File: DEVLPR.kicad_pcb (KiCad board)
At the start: 2 copper layers, 68.6 x 53.3 mm, 53 parts, among them CON1 SJ-3523-SMT-TR, J1 Conn_02x08_Row_Letter_Last, P1 Power, P2 Analog, P3 Digital, P4 Digital, P5 CONN_01X01, P6 CONN_01X01, P7 CONN_01X01, P8 CONN_01X01, U1 OPA140DGK, U2 INA333AIDGKR, U3 OPA376xxD, U4 TLV9002IPWR, U5 LM27761

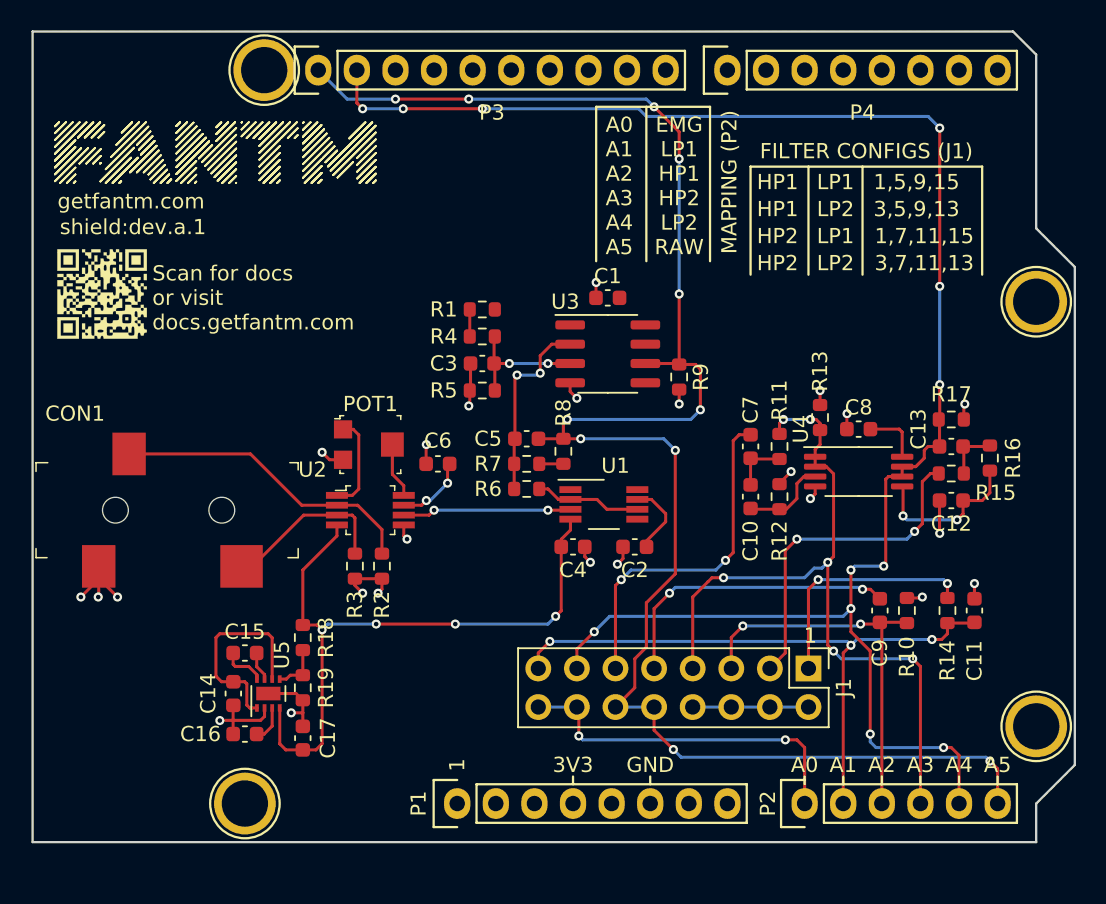
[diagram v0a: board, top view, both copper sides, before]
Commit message: Finalized rev dev.a.2 with improved filtering, power supply design, and silkscreen
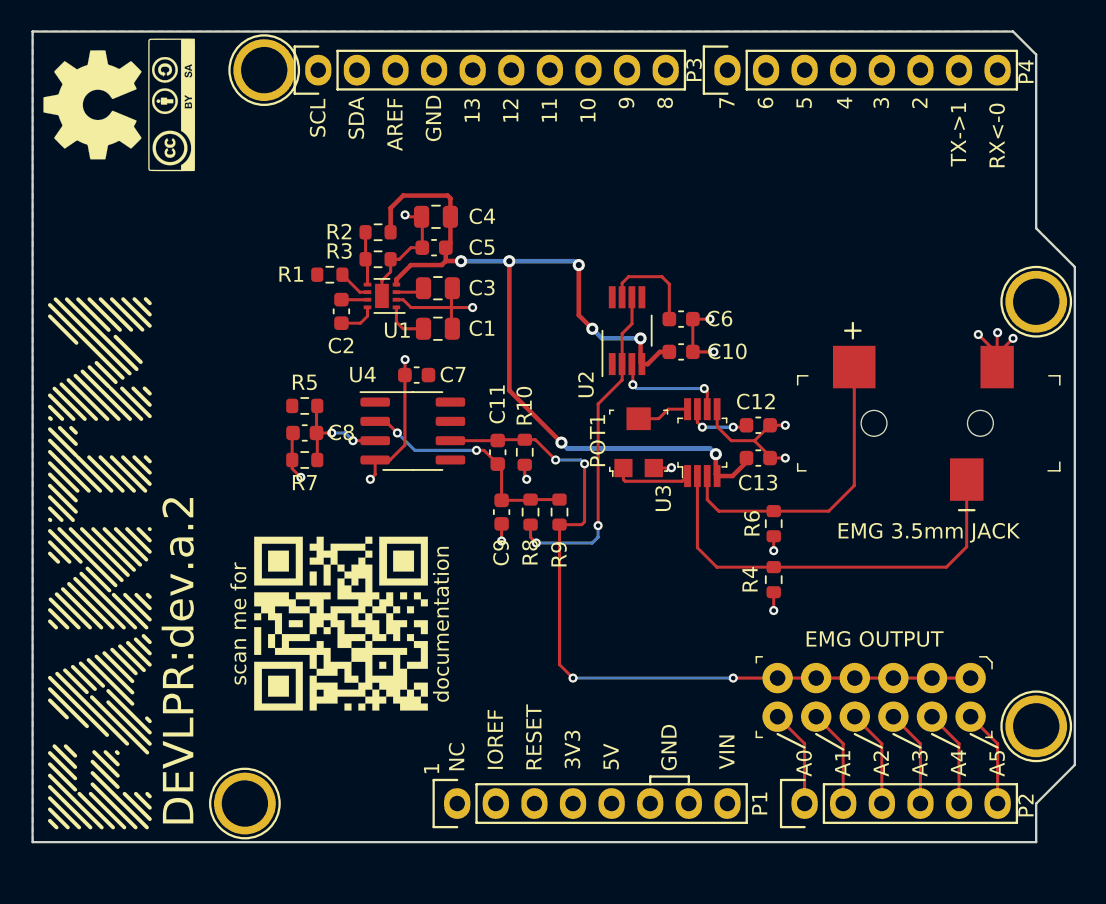
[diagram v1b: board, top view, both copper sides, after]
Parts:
- removed C14, C16: 4.7uF, Capacitor_SMD:C_0603_1608Metric
- removed C15: 1uF, Capacitor_SMD:C_0603_1608Metric
- removed C17: 2.2uF, Capacitor_SMD:C_0603_1608Metric
- removed the G*** at (115.6, 90.3)
- removed R11, R12, R19: 100k, Resistor_SMD:R_0603_1608Metric
- removed R13, R14, R15, R16, R17: 10k, Resistor_SMD:R_0603_1608Metric
- removed R18: 309k, Resistor_SMD:R_0603_1608Metric
- removed U5: LM27761, Package_SON:WSON-8-1EP_2x2mm_P0.5mm_EP0.9x1.6mm
- added G***: LOGO, kicad:qrcode_big, F.Cu at (131.3, 112.0)
- added G***: LOGO, kicad:cc_smlst, F.Cu at (120.1, 77.9)
- added G***: LOGO, kicad:oh_smlst, F.Cu at (114.9, 77.9)
- C1, C4: value 0.1uF -> 10uF; footprint Capacitor_SMD:C_0603_1608Metric -> Capacitor_SMD:C_0805_2012Metric
- C10, C7: value 0.15uF -> 0.1uF
- C11: value 0.033uF -> 4700pF
- C12, C13: value 0.033uF -> 0.1uF
- C2, C8: value 0.1uF -> 1uF
- C3: value 1uF -> 10uF; footprint Capacitor_SMD:C_0603_1608Metric -> Capacitor_SMD:C_0805_2012Metric
- C5: value 43pF -> 1uF
- C9: value 0.15uF -> 4700pF
- CON1: value SJ-3523-SMT-TR -> EMG 3.5mm JACK
- J1: value Conn_02x08_Row_Letter_Last -> EMG OUTPUT; footprint Connector_PinHeader_2.54mm:PinHeader_2x08_P2.54mm_Vertical -> digikey-footprints:PinHeader_6x2_P2.54mm_Horizontal
- POT1: value TC33X-2-103E -> GAIN
- R1: value 33k -> 100k
- R10: value 100k -> 10k
- R2: value 47k -> 182k
- R3: value 47k -> 100k
- R4: value 3.9k -> 47k
- R5: value 10k -> 36.5k
- R6: value 39k -> 47k
- R7: value 33k -> 10k
- R8: value 2.7k -> 39k
- R9: value 10k -> 35.7k
- U1: value OPA140DGK -> LM27761; footprint Package_SO:VSSOP-8_3.0x3.0mm_P0.65mm -> Package_SON:WSON-8-1EP_2x2mm_P0.5mm_EP0.9x1.6mm
- U2: value INA333AIDGKR -> OPA140DGK; footprint digikey-footprints:TSSOP-8_W3mm -> Package_SO:VSSOP-8_3.0x3.0mm_P0.65mm
- U3: value OPA376xxD -> INA333AIDGKR; footprint Package_SO:SOIC-8_3.9x4.9mm_P1.27mm -> digikey-footprints:TSSOP-8_W3mm
- U4: value TLV9002IPWR -> OPA376xxD; footprint Package_SO:TSSOP-8_4.4x3mm_P0.65mm -> Package_SO:SOIC-8_3.9x4.9mm_P1.27mm
- moved CON1 55.4 mm to (172.5, 98.8), turned to 180 degrees
- moved C8 36.4 mm to (128.9, 99.4)
- moved C11 33.1 mm to (141.6, 100.7)
- moved U4 29.5 mm to (136.0, 99.3)
- moved R10 27.2 mm to (143.4, 100.7), turned to 270 degrees
- moved C9 25.7 mm to (141.9, 104.6)
- moved R4 25.0 mm to (159.8, 109.1), turned to 90 degrees
- moved C2 24.8 mm to (131.3, 91.4), turned to 270 degrees
- moved C4 23.5 mm to (137.5, 85.2)
- moved C7 22.5 mm to (136.3, 95.6), turned to 0 degrees
- moved R2 22.0 mm to (133.7, 86.2), turned to 180 degrees
- moved U2 20.6 mm to (150.1, 92.7), turned to 90 degrees
- moved R3 20.3 mm to (133.7, 88.0), turned to 0 degrees
- moved U1 20.0 mm to (134.0, 90.4), turned to 180 degrees
- moved C6 18.6 mm to (153.7, 91.9), turned to 180 degrees
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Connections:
- C1 pad 1: GND -> +5V
- C1 pad 2: +5V -> GND
- C10 pad 1: /EMG Amplifiers/HP_2_+ -> GND
- C10 pad 2: /EMG Amplifiers/HP_2_MID -> -4V5
- C11 pad 1: GND -> /EMG_OUT
- C11 pad 2: /A1 -> Net-(C11-Pad2)
- C12 pad 2: /EMG Amplifiers/LP_2_+ -> +5V
- C13 pad 1: /EMG Amplifiers/LP_2_MID -> GND
- C13 pad 2: /A4(SDA) -> -4V5
- C2 pad 1: GND -> /-5V Source/C-
- C2 pad 2: +5V -> /-5V Source/C+
- C3 pad 1: GND -> /-5V Source/CPOUT
- C3 pad 2: Net-(C3-Pad2) -> GND
- C4 pad 1: GND -> -4V5
- C4 pad 2: -5V -> GND
- C5 pad 1: /A5(SCL) -> GND
- C5 pad 2: Net-(C5-Pad2) -> -4V5
- C7 pad 1: /EMG Amplifiers/HP_2_MID -> GND
- C7 pad 2: /EMG Amplifiers/SECOND_ORDER_HP -> +5V
- C8 pad 2: +5V -> Net-(C8-Pad2)
- C9 pad 1: /A2 -> GND
- C9 pad 2: /EMG Amplifiers/FIRST_ORDER_HP -> Net-(C11-Pad2)
- J1 pad 1: /EMG Amplifiers/FIRST_ORDER_LP -> /EMG_OUT
- J1 pad 10: /A5(SCL) -> /A1
- J1 pad 11: /EMG Amplifiers/SECOND_ORDER_HP -> /EMG_OUT
- J1 pad 12: /A5(SCL) -> /A0
- J1 pad 2: /EMG Amplifiers/HP -> /A5(SCL)
- J1 pad 3: /EMG Amplifiers/SECOND_ORDER_LP -> /EMG_OUT
- J1 pad 4: /EMG Amplifiers/HP -> /A4(SDA)
- J1 pad 5: /A2 -> /EMG_OUT
- J1 pad 6: /EMG Amplifiers/HP -> /A3
- J1 pad 7: /A3 -> /EMG_OUT
- J1 pad 8: /EMG Amplifiers/HP -> /A2
- J1 pad 9: /EMG Amplifiers/FIRST_ORDER_HP -> /EMG_OUT
- R10 pad 1: /A2 -> /EMG_OUT
- R2 pad 1: GND -> -4V5
- R2 pad 2: /EMG_N -> /-5V Source/VFB
- R3 pad 1: GND -> /-5V Source/VFB
- R3 pad 2: /EMG_P -> GND
- R4 pad 1: Net-(C3-Pad2) -> GND
- R4 pad 2: Net-(R1-Pad1) -> /EMG_N
- R5 pad 1: Net-(C3-Pad2) -> Net-(C8-Pad2)
- R5 pad 2: GND -> +5V
- R6 pad 1: Net-(C5-Pad2) -> GND
- R6 pad 2: Net-(R6-Pad2) -> /EMG_P
- R7 pad 1: Net-(R7-Pad1) -> Net-(C8-Pad2)
- R7 pad 2: Net-(C5-Pad2) -> GND
- R8 pad 1: /A5(SCL) -> Net-(C11-Pad2)
- R8 pad 2: Net-(R7-Pad1) -> Net-(R8-Pad2)
- R9 pad 1: /A5(SCL) -> /EMG_OUT
- R9 pad 2: GND -> Net-(C11-Pad2)
- U1 pad 1: (no net) -> +5V
- U1 pad 2: Net-(R6-Pad2) -> GND
- U1 pad 3: /EMG Amplifiers/EMG_INSTR -> /-5V Source/CPOUT
- U1 pad 4: -5V -> -4V5
- U1 pad 5: (no net) -> /-5V Source/VFB
- U1 pad 6: Net-(R6-Pad2) -> Net-(R1-Pad1)
- U1 pad 7: +5V -> /-5V Source/C-
- U1 pad 8: (no net) -> /-5V Source/C+
- U2 pad 1: Net-(POT1-Pad1) -> (no net)
- U2 pad 2: /EMG_N -> Net-(R8-Pad2)
- U2 pad 3: /EMG_P -> /EMG Amplifiers/EMG_INSTR
- U2 pad 4: -5V -> -4V5
- U2 pad 5: GND -> (no net)
- U2 pad 6: /EMG Amplifiers/EMG_INSTR -> Net-(R8-Pad2)
- U2 pad 8: Net-(POT1-Pad2) -> (no net)
- U3 pad 1: Net-(U3-Pad1) -> Net-(POT1-Pad1)
- U3 pad 2: Net-(C5-Pad2) -> /EMG_N
- U3 pad 3: Net-(C3-Pad2) -> /EMG_P
- U3 pad 4: GND -> -4V5
- U3 pad 5: Net-(U3-Pad5) -> GND
- U3 pad 6: /A5(SCL) -> /EMG Amplifiers/EMG_INSTR
- U3 pad 8: Net-(U3-Pad8) -> Net-(POT1-Pad2)
- U4 pad 1: /A3 -> Net-(U4-Pad1)
- U4 pad 2: /A3 -> Net-(C11-Pad2)
- U4 pad 3: /EMG Amplifiers/HP_2_+ -> Net-(C8-Pad2)
- U4 pad 5: /EMG Amplifiers/LP_2_+ -> Net-(U4-Pad5)
- U4 pad 6: /A4(SDA) -> /EMG_OUT
- U4 pad 7: /A4(SDA) -> +5V
- U4 pad 8: +5V -> Net-(U4-Pad8)
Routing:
- net /A4(SDA): track 117.0 -> 6.45 mm, vias 12 -> 0
- net /A5(SCL): track 115.4 -> 6.45 mm, vias 11 -> 0
- net -4V5: track 0.00 -> 62.9 mm, vias 0 -> 7
- net /EMG_OUT: track 0.00 -> 51.7 mm, vias 0 -> 4
- net -5V: track 44.4 -> 0.00 mm, vias 4 -> 0
- net /A3: track 49.6 -> 6.45 mm, vias 6 -> 0
- net /A1: track 41.8 -> 6.45 mm, vias 3 -> 0
- net /EMG Amplifiers/SECOND_ORDER_HP: track 22.8 -> 0.00 mm, vias 2 -> 0
- net Net-(R8-Pad2): track 0.00 -> 22.3 mm, vias 0 -> 2
- net /EMG Amplifiers/SECOND_ORDER_LP: track 22.0 -> 0.00 mm, vias 2 -> 0
- net /EMG Amplifiers/FIRST_ORDER_HP: track 19.7 -> 0.00 mm, vias 2 -> 0
- net /A2: track 26.0 -> 6.45 mm, vias 2 -> 0
- net /A0: track 23.4 -> 6.45 mm, vias 2 -> 0
- net /EMG Amplifiers/FIRST_ORDER_LP: track 15.7 -> 0.00 mm, vias 2 -> 0
- net Net-(C11-Pad2): track 0.00 -> 15.5 mm, vias 0 -> 2
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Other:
- net class Power added: clearance 0, trace_width 0.3, via_dia 0.8, via_drill 0.4
- board text added: "10"
- board text added: "11"
- board text added: "12"
- board text added: "13"
- board text added: "2"
- board text added: "3"
- board text added: "4"
- board text added: "5"
- board text added: "5V"
- board text added: "6"
- board text added: "7"
- board text added: "8"
- board text added: "9"
- board text added: "AREF"
- board text added: "DEVLPR:dev.a.2"
- board text added: "IOREF"
- board text added: "NC"
- board text added: "RESET"
- board text added: "RX<-0"
- board text added: "SCL"
- board text added: "SDA"
- board text added: "TX->1"
- board text added: "VIN"
- board text removed: "1,5,9,15"
- board text removed: "1,7,11,15"
- board text removed: "3,5,9,13"
- board text removed: "3,7,11,13"
- board text removed: "A0 A1 A2 A3 A4 A5"
- board text removed: "EMG LP1 HP1 HP2 LP2 RAW"
- board text removed: "FILTER CONFIGS (J1)"
- board text removed: "HP1"
- board text removed: "HP2"
- board text removed: "LP1"
- board text removed: "LP2"
- board text removed: "MAPPING (P2)"
- board text removed: "Scan for docs or visit docs.getfantm.com"
- board text removed: "getfantm.com"
- board text removed: "shield:dev.a.1"

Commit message: Fixed SPI signal naming convention to new OSHWA proposal
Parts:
- removed the C11 at (141.6, 100.7)
- removed the C6 at (153.7, 91.9)
- removed G***: LOGO, kicad:qrcode_big
- removed G***: LOGO, kicad:cc_smlst
- removed G***: LOGO, kicad:oh_smlst
- removed the R1 at (130.6, 89.0)
- removed the R3 at (133.7, 88.0)
- removed the R5 at (128.9, 97.7)
- added C13: 1uF, Capacitor_SMD:C_0805_2012Metric, F.Cu at (146.3, 86.8)
- added C8: 6800pF, Capacitor_SMD:C_0603_1608Metric, F.Cu at (132.7, 107.5)
- added TP1: -3V, digikey-footprints:Test_Point_D1.02mm, F.Cu at (159.3, 82.8)
- added TP2: RAW_EMG, digikey-footprints:Test_Point_D1.02mm, F.Cu at (159.3, 90.7)
- added U4: INA818IDR, digikey-footprints:SOIC-8_W3.9mm, F.Cu at (153.9, 100.5)
- C1, C3, C4: value 10uF -> 1uF
- C10: value 0.1uF -> 6800pF
- C2: footprint Capacitor_SMD:C_0603_1608Metric -> Capacitor_SMD:C_0805_2012Metric
- C5: value 1uF -> 0.1uF
- C9: value 4700pF -> 0.1uF
- CON1: value EMG 3.5mm JACK -> SJ-3523-SMT-TR
- R2: value 182k -> 25.5k
- R5: renamed from R8; value 39k -> 46.4k
- U1: value LM27761 -> TPS60403; footprint Package_SON:WSON-8-1EP_2x2mm_P0.5mm_EP0.9x1.6mm -> Package_TO_SOT_SMD:SOT-23-5
- U2: value OPA140DGK -> MAX1735; footprint Package_SO:VSSOP-8_3.0x3.0mm_P0.65mm -> Package_TO_SOT_SMD:SOT-23-5
- U3: value INA333AIDGKR -> OPA375DCK; footprint digikey-footprints:TSSOP-8_W3mm -> digikey-footprints:SC-70-5
- moved C5 23.9 mm to (143.1, 110.4), turned to 180 degrees
- moved C10 22.0 mm to (136.3, 107.5), turned to 270 degrees
- moved C4 15.3 mm to (152.7, 86.8), turned to 270 degrees
- moved U3 13.9 mm to (143.1, 107.3), turned to 90 degrees
- moved R2 12.4 mm to (128.9, 97.7)
- moved C2 11.9 mm to (140.5, 83.8), turned to 180 degrees
- moved R6 11.5 mm to (134.5, 107.5), turned to 270 degrees
- moved C6 7.43 mm to (136.1, 103.1)
- moved U1 7.36 mm to (140.5, 86.9), turned to 270 degrees
- moved C3 7.07 mm to (144.0, 86.8), turned to 90 degrees
- moved R5 6.39 mm to (138.0, 107.5), turned to 90 degrees
- moved U2 5.81 mm to (149.5, 86.9), turned to 270 degrees
- moved C1 5.53 mm to (137.4, 87.1), turned to 90 degrees
- moved POT1 2.41 mm to (148.5, 99.9)
- moved R7 2.35 mm to (141.0, 100.8)
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- renumbered C12 to C11, C13 to C12, C7 to C6, C8 to C7, R4 to R1, R6 to R3, R7 to R4, R9 to R6, R10 to R7, U4 to U5
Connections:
- net /10(**/SS) renamed /10(**|CS)
- net /11(**/MOSI) renamed /11(**|SDO)
- net /12(MISO) renamed /12(SDI)
- C1 pad 1: +5V -> GND
- C1 pad 2: GND -> +5V
- C10 pad 1: GND -> /EMG_OUT
- C10 pad 2: -4V5 -> /EMG Amplifiers/BUFFER_OUT
- C12 pad 2: -4V5 -> -3V
- C2 pad 1: /-5V Source/C- -> /-5V Source/Cfly+
- C2 pad 2: /-5V Source/C+ -> /-5V Source/Cfly-
- C3 pad 1: /-5V Source/CPOUT -> GND
- C3 pad 2: GND -> /-5V Source/-5V
- C4 pad 1: -4V5 -> GND
- C4 pad 2: GND -> -3V
- C5 pad 2: -4V5 -> +5V
- C7 pad 2: Net-(C8-Pad2) -> /EMG Amplifiers/V_SHIFT
- C9 pad 2: Net-(C11-Pad2) -> -3V
- POT1 pad 1: Net-(POT1-Pad1) -> /EMG Amplifiers/RG_1
- POT1 pad 2: Net-(POT1-Pad2) -> /EMG Amplifiers/RG_2
- R2 pad 1: -4V5 -> /EMG Amplifiers/V_SHIFT
- R2 pad 2: /-5V Source/VFB -> +5V
- R4 pad 1: Net-(C8-Pad2) -> /EMG Amplifiers/V_SHIFT
- R5 pad 1: Net-(C11-Pad2) -> /EMG Amplifiers/BUFFER_OUT
- R5 pad 2: Net-(R8-Pad2) -> /EMG Amplifiers/BUFFER_FDBK
- R6 pad 2: Net-(C11-Pad2) -> /EMG Amplifiers/BUFFER_OUT
- U1 pad 1: +5V -> /-5V Source/-5V
- U1 pad 2: GND -> +5V
- U1 pad 3: /-5V Source/CPOUT -> /-5V Source/Cfly-
- U1 pad 4: -4V5 -> GND
- U1 pad 5: /-5V Source/VFB -> /-5V Source/Cfly+
- U2 pad 1: (no net) -> GND
- U2 pad 2: Net-(R8-Pad2) -> /-5V Source/-5V
- U2 pad 3: /EMG Amplifiers/EMG_INSTR -> /-5V Source/-5V
- U2 pad 4: -4V5 -> GND
- U2 pad 5: (no net) -> -3V
- U3 pad 1: Net-(POT1-Pad1) -> /EMG Amplifiers/EMG_INSTR
- U3 pad 2: /EMG_N -> -3V
- U3 pad 3: /EMG_P -> /EMG Amplifiers/BUFFER_FDBK
- U3 pad 4: -4V5 -> /EMG Amplifiers/BUFFER_FDBK
- U3 pad 5: GND -> +5V
- U5 pad 2: Net-(C11-Pad2) -> /EMG Amplifiers/BUFFER_OUT
- U5 pad 3: Net-(C8-Pad2) -> /EMG Amplifiers/V_SHIFT
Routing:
- net -3V: track 0.00 -> 71.7 mm, vias 0 -> 6
- net -4V5: track 62.9 -> 0.00 mm, vias 7 -> 0
- net /EMG Amplifiers/EMG_INSTR: track 7.62 -> 35.3 mm, vias 2 -> 3
- net Net-(R8-Pad2): track 22.3 -> 0.00 mm, vias 2 -> 0
- net /EMG Amplifiers/BUFFER_OUT: track 0.00 -> 18.2 mm
- net /-5V Source/-5V: track 0.00 -> 15.8 mm
- net Net-(C11-Pad2): track 15.5 -> 0.00 mm, vias 2 -> 0
- net /EMG Amplifiers/V_SHIFT: track 0.00 -> 7.67 mm, vias 0 -> 2
- net Net-(C8-Pad2): track 7.67 -> 0.00 mm, vias 2 -> 0
- net /EMG_OUT: track 51.7 -> 58.6 mm, vias 4 -> 3
- net /EMG Amplifiers/RG_1: track 0.00 -> 6.88 mm
- net /EMG Amplifiers/BUFFER_FDBK: track 0.00 -> 6.25 mm, vias 0 -> 2
- net /-5V Source/Cfly+: track 0.00 -> 6.06 mm
- net +5V: track 13.9 -> 19.2 mm, vias 2 -> 0
- net Net-(POT1-Pad1): track 5.16 -> 0.00 mm
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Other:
- board text added: "DEVLPR:dev.a.3"
- board text removed: "DEVLPR:dev.a.2"
